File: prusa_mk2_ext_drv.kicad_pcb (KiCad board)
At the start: 2 copper layers, 69 x 43 mm, 38 parts, among them CN1 FAN, CN2 MiniRambo, CN3 X_MOT, CN4 Y_MOT, J1 DirRevX, J2 DirRevY, J3 CfgX, J4 CfgY, Q1 BC546, Q2 BC546

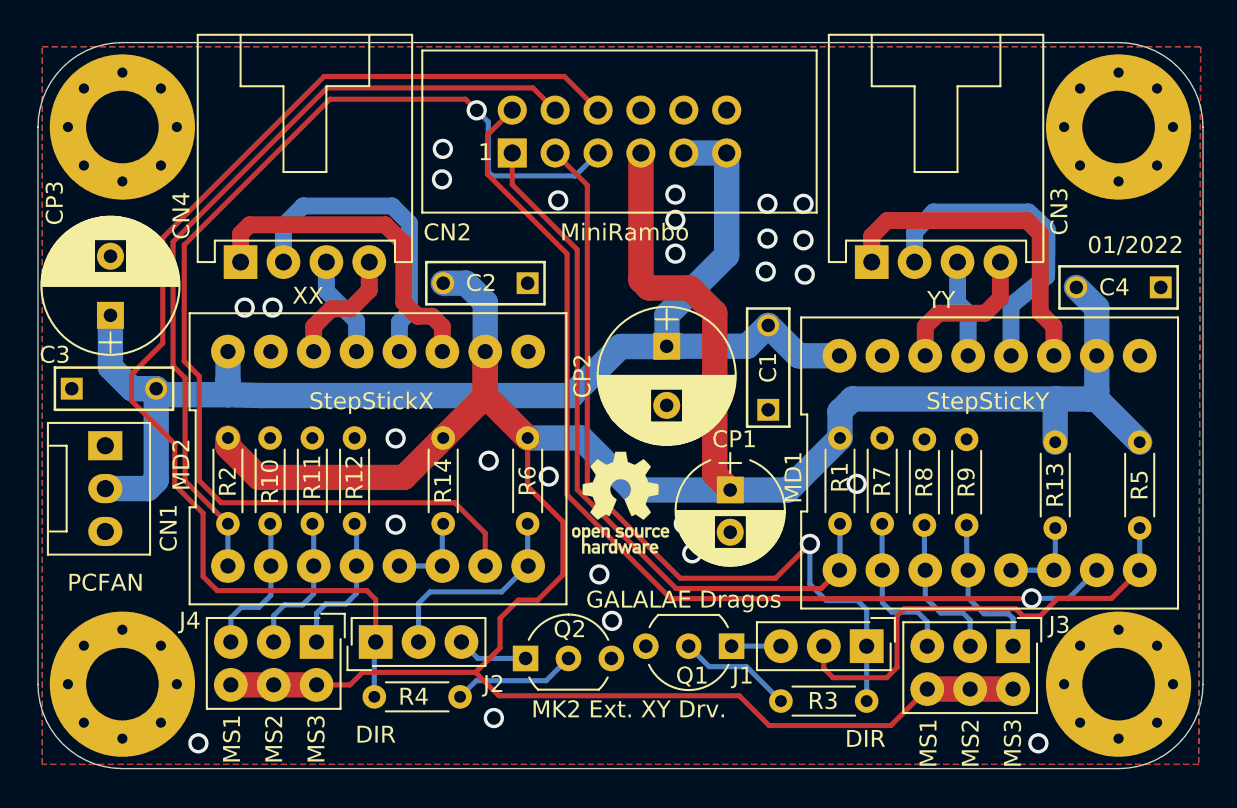
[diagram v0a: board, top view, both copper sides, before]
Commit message: Initial version was sent to manufacturing, also made cosmetic changes and DRC with the new KiCAD v.6.0
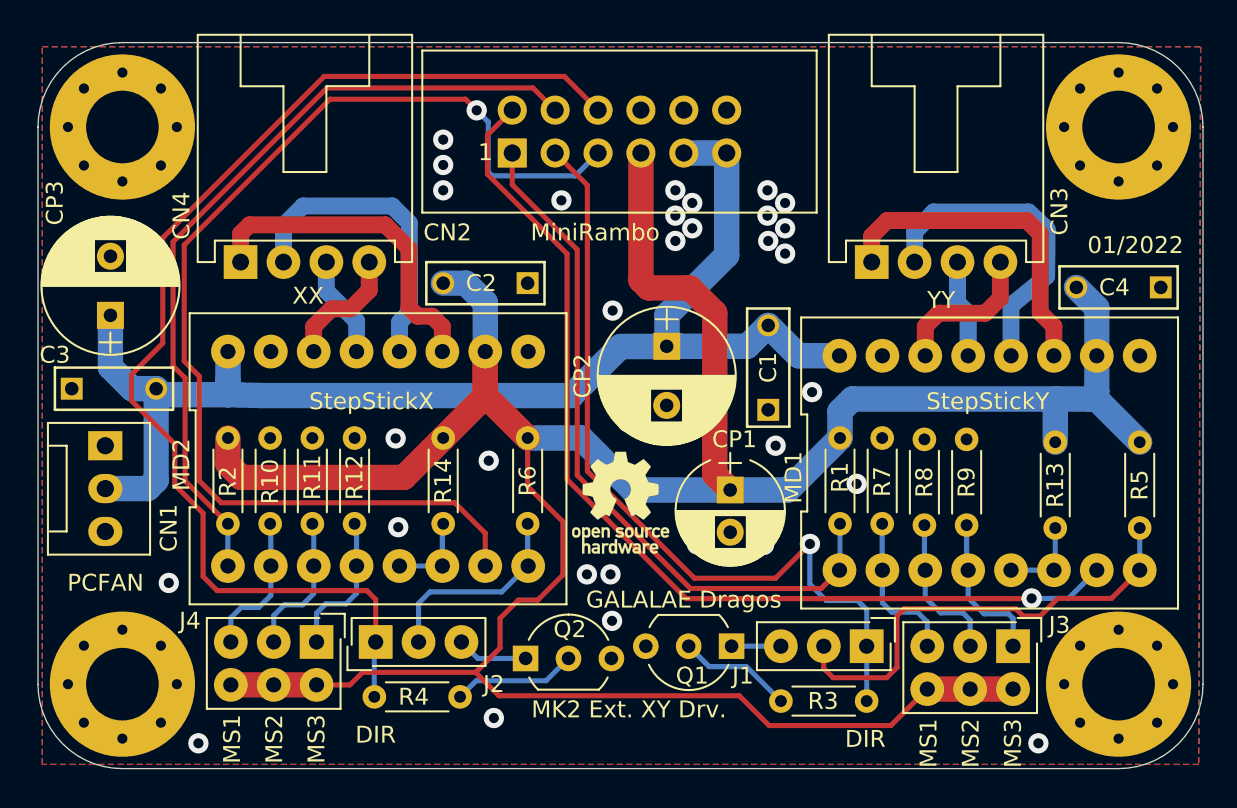
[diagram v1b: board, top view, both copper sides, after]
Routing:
- net +5V: track 174.8 -> 175.4 mm
- net Net-(CN2-Pad2): track 60.0 -> 59.4 mm
- net GND: vias 28 -> 35
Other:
- net class Default removed
- net class Mot_volts removed
- net class Mot_wire removed
